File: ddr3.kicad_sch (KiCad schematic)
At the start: 26 parts, among them U11 LIFCL-40-9BG256C, U12 MT41K128M16JT-125_K

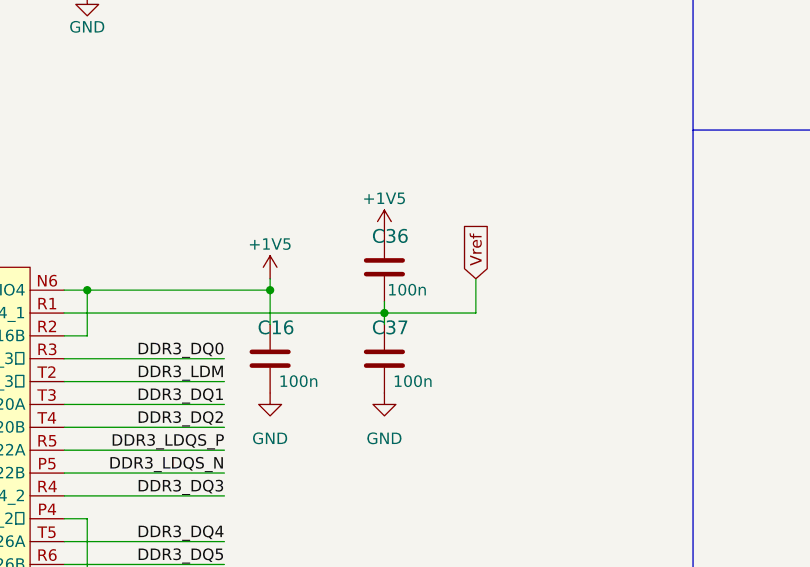
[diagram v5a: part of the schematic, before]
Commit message: Finished component placement
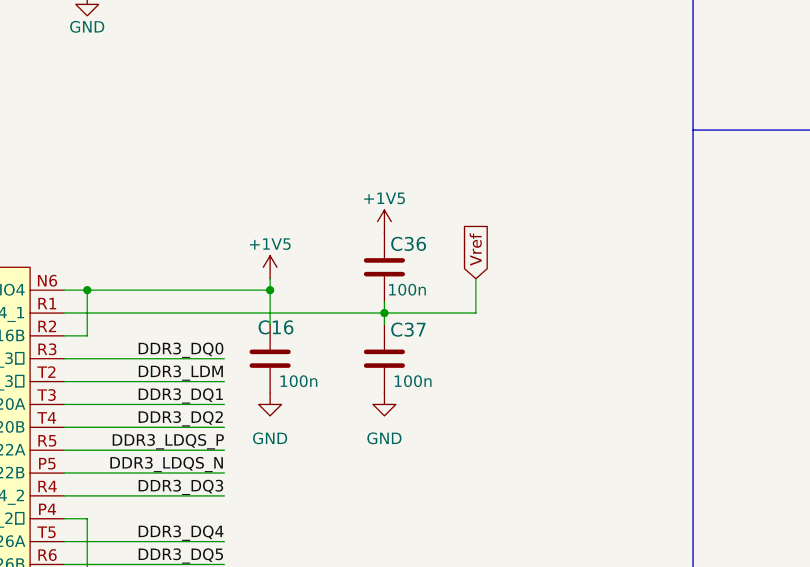
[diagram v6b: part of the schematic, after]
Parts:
- removed R43: R_100R_0402, crosslink-nx-video-converter-footprints:0402-res, symbol crosslink-nx-video-converter:R_100R_0402
- added R43: R_100R_0201, antmicro-footprints:0201-res, symbol antmicroResistorsmisc:R_100R_0201
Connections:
- net DDR3_CK_N: now also R43.1
- net DDR3_CK_P: now also R43.2
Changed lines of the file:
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@@
     (pin "8")
-  )
-  (symbol (lib_id "crosslink-nx-video-converter:R_100R_0402") (at 190.5 83.82 90) (unit 1)
-    (in_bom yes) (on_board yes) (fields_autoplaced)
-    (property "Reference" "R43" (id 0) (at 193.04 82.55 90)
-      (effects (font (size 1.524 1.524)) (justify right))
-    )
-    (property "Value" "R_100R_0402" (id 1) (at 194.31 83.82 0)
-      (effects (font (size 1.524 1.524)) hide)
-    )
-    (property "Footprint" "crosslink-nx-video-converter-footprints:0402-res" (id 2) (at 185.42 78.74 0)
-      (effects (font (size 1.524 1.524)) (justify left) hide)
-    )
-    (property "Datasheet" "" (id 3) (at 190.5 83.82 0)
-      (effects (font (size 1.27 1.27)) hide)
-    )
-    (property "Manufacturer" "BOURNS" (id 4) (at 180.34 78.74 0)
-      (effects (font (size 1.524 1.524)) (justify left) hide)
-    )
-    (property "MPN" "CR0402-FX-1000GLF" (id 5) (at 182.88 78.74 0)
-      (effects (font (size 1.524 1.524)) (justify left) hide)
-    )
-    (property "Val" "100R" (id 6) (at 193.04 85.7249 90)
-      (effects (font (size 1.27 1.27)) (justify right))
-    )
-    (pin "1")
-    (pin "2")
   )
   (symbol (lib_id "antmicroCapacitors0402:C_100n_0402") (at 130.81 181.61 0) (unit 1)
     (in_bom yes) (on_board yes)
-    (property "Reference" "C37" (id 0) (at 129.413 178.181 0)
+    (property "Reference" "C37" (id 0) (at 131.445 178.435 0)
       (effects (font (size 1.524 1.524)) (justify left))
     )
@@
     (pin "8")
   )
+  (symbol (lib_id "antmicroResistorsmisc:R_100R_0201") (at 190.5 83.82 90) (unit 1)
+    (in_bom yes) (on_board yes) (fields_autoplaced)
+    (property "Reference" "R43" (id 0) (at 193.04 82.55 90)
+      (effects (font (size 1.524 1.524)) (justify right))
+    )
+    (property "Value" "R_100R_0201" (id 1) (at 198.12 83.82 0)
+      (effects (font (size 1.524 1.524)) hide)
+    )
+    (property "Footprint" "antmicro-footprints:0201-res" (id 2) (at 205.74 95.25 0)
+      (effects (font (size 1.524 1.524)) (justify left) hide)
+    )
+    (property "Datasheet" "https://www.mouser.pl/datasheet/2/54/cr_a_as-1858644.pdf" (id 3) (at 195.58 83.82 0)
+      (effects (font (size 1.27 1.27)) hide)
+    )
+    (property "Manufacturer" "Bourns" (id 4) (at 200.66 95.25 0)
+      (effects (font (size 1.524 1.524)) (justify left) hide)
+    )
+    (property "MPN" "CR0201AFW-1000GAS " (id 5) (at 203.2 95.25 0)
+      (effects (font (size 1.524 1.524)) (justify left) hide)
+    )
+    (property "Val" "100R" (id 6) (at 193.04 85.7249 90)
+      (effects (font (size 1.27 1.27)) (justify right))
+    )
+    (pin "1")
+    (pin "2")
+  )
   (symbol (lib_id "power:GND") (at 295.91 87.63 0) (unit 1)
     (in_bom yes) (on_board yes) (fields_autoplaced)
@@
   (symbol (lib_id "antmicroCapacitors0402:C_100n_0402") (at 130.81 171.45 0) (unit 1)
     (in_bom yes) (on_board yes)
-    (property "Reference" "C36" (id 0) (at 129.413 168.021 0)
+    (property "Reference" "C36" (id 0) (at 131.445 168.91 0)
       (effects (font (size 1.524 1.524)) (justify left))
     )

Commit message: Loclib
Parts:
- C16, C35, C36, C37, C38, C39: footprint antmicro-footprints:0402-cap -> crosslink-nx-video-converter-footprints:0402-cap; symbol antmicroCapacitors0402:C_100n_0402 -> crosslink-nx-video-converter:C_100n_0402
- R43: footprint antmicro-footprints:0201-res -> crosslink-nx-video-converter-footprints:0201-res; symbol antmicroResistorsmisc:R_100R_0201 -> crosslink-nx-video-converter:R_100R_0201
- U11: footprint antmicro-footprints:BGA-256_16x16_14.0x14.0mm -> crosslink-nx-video-converter-footprints:BGA-256_16x16_14.0x14.0mm; symbol antmicroBGAchips:LIFCL-40-9BG256C -> crosslink-nx-video-converter:LIFCL-40-9BG256C
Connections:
- net +1V5: no longer U11.P11 (PB54B/PCLKC3_0/ADC_CN5 ), U11.P12 (VCCIO3)
- net DDR3_A0: no longer U11.N13 (PB70B/COMP2IN )
- net DDR3_A1: no longer U11.P15 (PB72A/PCLKT3_2/ADC_CP13)
- net DDR3_A10: no longer U11.L12 (PB82B/ADC_CN15)
- net DDR3_A11: no longer U11.M16 (PB84A/LRC_GPLL0T_IN)
- net DDR3_A2: no longer U11.P16 (PB72B/PCLKC3_2/ADC_CN13)
- net DDR3_A3: no longer U11.M14 (PB74A/PCLKT3_3/ADC_CP14)
- net DDR3_A4: no longer U11.N16 (PB76A/COMP3IP)
- net DDR3_A5: no longer U11.N15 (PB76B/COMP3IN)
- net DDR3_A6: no longer U11.M12 (PB78A/ADC_CP11)
- net DDR3_A7: no longer U11.L11 (PB80A/ADC_CP12)
- net DDR3_A8: no longer U11.L10 (PB80B/ADC_CN12)
- net DDR3_A9: no longer U11.M13 (PB82A/ADC_CP15)
- net DDR3_DQ10: no longer U11.T11 (PB58B/PCLKC3_1/ADC_CN6 )
- net DDR3_DQ11: no longer U11.R13 (PB62A/ADC_CP10)
- net DDR3_DQ12: no longer U11.R14 (PB62B/ADC_CN10)
- net DDR3_DQ13: no longer U11.T14 (PB66A/COMP1IP)
- net DDR3_DQ14: no longer U11.T15 (PB66B/COMP1IN)
- net DDR3_DQ15: no longer U11.R16 (PB68A/ADC_CP8)
- net DDR3_DQ8: no longer U11.R10 (PB56B/ADC_CN7 )
- net DDR3_DQ9: no longer U11.T12 (PB58A/PCLKT3_1/ADC_CP6 )
- net DDR3_UDM: no longer U11.R15 (PB68B/ADC_CN8)
- net DDR3_UDQS_N: no longer U11.T13 (PB60B/ADC_CN9)
- net DDR3_UDQS_P: no longer U11.R12 (PB60A/ADC_CP9)
- net GND: no longer U11.M11 (PB78B/ADC_CN11), U11.M15 (PB84B/LRC_GPLL0C_IN/VREF3_2), U11.N11 (PB64B/ADC_CN4), U11.N12 (PB64A/ADC_CP4), U11.N14 (PB74B/PCLKC3_3/ADC_CN14), U11.P10 (PB56A/ADC_CP7 ), U11.P14 (PB70A/COMP2IP)
- net Vref: no longer U11.R11 (PB54A/PCLKT3_0/VREF3_1/ADC_CP5)

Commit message: Routed DDR3 C&A
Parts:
- removed unit 4 of U11
- added unit 4 of U11
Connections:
- net +1V5: now also U11.P11 (PB54B/PCLKC3_0/ADC_CN5 ), U11.P12 (VCCIO3)
- net DDR3_A0: now also R49.4, U11.P8 (PB42B); no longer R44.1
- net DDR3_A1: now also R46.4, U11.N16 (PB76A/COMP3IP); no longer R44.2
- net DDR3_A10: now also R46.1, U11.P15 (PB72A/PCLKT3_2/ADC_CP13); no longer R46.3
- net DDR3_A11: now also R48.2, U11.M14 (PB74A/PCLKT3_3/ADC_CP14); no longer R46.4
- net DDR3_A12: now also R46.2, U11.N15 (PB76B/COMP3IN); no longer R48.1, U11.T7 (PB30A)
- net DDR3_A13: now also R49.1, U11.L11 (PB80A/ADC_CP12); no longer R48.2, U11.T8 (PB30B)
- net DDR3_A2: now also R49.2, U11.N8 (PB36A); no longer R44.3
- net DDR3_A3: now also R49.3, U11.P7 (PB32B); no longer R44.4
- net DDR3_A4: now also R48.1, U11.M16 (PB84A/LRC_GPLL0T_IN); no longer R45.1
- net DDR3_A5: now also R45.1, U11.N9 (PB36B); no longer R45.2
- net DDR3_A6: now also R48.3, U11.M13 (PB82A/ADC_CP15); no longer R45.3
- net DDR3_A7: now also R45.2, U11.L10 (PB80B/ADC_CN12); no longer R45.4
- net DDR3_A8: now also R48.4, U11.L12 (PB82B/ADC_CN15); no longer R46.1
- net DDR3_A9: now also R45.4, U11.L8 (PB34A); no longer R46.2
- net DDR3_BA0: now also R44.1, U11.P9 (PB44B/PCLKC4_0); no longer R48.3, U11.P6 (PB32A)
- net DDR3_BA1: now also R46.3, U11.P16 (PB72B/PCLKC3_2/ADC_CN13); no longer R48.4, U11.P7 (PB32B)
- net DDR3_BA2: now also R44.2, U11.M10 (PB46A); no longer R50.4, U11.L8 (PB34A)
- net DDR3_CKE: now also R50.4, U11.N13 (PB70B/COMP2IN ); no longer R50.3, U11.P9 (PB44B/PCLKC4_0)
- net DDR3_DQ0: now also U11.T4 (PB20B); no longer U11.R3 (PB18A/PCLKT4_3 )
- net DDR3_DQ1: now also U11.T6 (PB28A); no longer U11.T3 (PB20A)
- net DDR3_DQ10: now also U11.T15 (PB66B/COMP1IN)
- net DDR3_DQ11: now also U11.R13 (PB62A/ADC_CP10)
- net DDR3_DQ12: now also U11.R14 (PB62B/ADC_CN10)
- net DDR3_DQ13: now also U11.R10 (PB56B/ADC_CN7 )
- net DDR3_DQ14: now also U11.R15 (PB68B/ADC_CN8)
- net DDR3_DQ15: now also U11.T11 (PB58B/PCLKC3_1/ADC_CN6 )
- net DDR3_DQ2: now also U11.R3 (PB18A/PCLKT4_3 ); no longer U11.T4 (PB20B)
- net DDR3_DQ3: now also U11.R6 (PB26B); no longer U11.R4 (PB24A/PCLKT4_2)
- net DDR3_DQ4: now also U11.T2 (PB18B/PCLKC4_3 ); no longer U11.T5 (PB26A)
- net DDR3_DQ5: now also U11.R4 (PB24A/PCLKT4_2); no longer U11.R6 (PB26B)
- net DDR3_DQ6: now also U11.T3 (PB20A); no longer U11.T6 (PB28A)
- net DDR3_DQ7: now also U11.T5 (PB26A); no longer U11.R7 (PB28B)
- net DDR3_DQ8: now also U11.R16 (PB68A/ADC_CP8)
- net DDR3_DQ9: now also U11.T12 (PB58A/PCLKT3_1/ADC_CP6 )
- net DDR3_LDM: now also U11.R7 (PB28B); no longer U11.T2 (PB18B/PCLKC4_3 )
- net DDR3_ODT: now also R50.1, U11.T7 (PB30A); no longer R50.2, U11.M10 (PB46A)
- net DDR3_UDM: now also U11.T14 (PB66A/COMP1IP)
- net DDR3_UDQS_N: now also U11.T13 (PB60B/ADC_CN9)
- net DDR3_UDQS_P: now also U11.R12 (PB60A/ADC_CP9)
- net GND: now also U11.M11 (PB78B/ADC_CN11), U11.M15 (PB84B/LRC_GPLL0C_IN/VREF3_2), U11.N11 (PB64B/ADC_CN4), U11.N12 (PB64A/ADC_CP4), U11.N14 (PB74B/PCLKC3_3/ADC_CN14), U11.P10 (PB56A/ADC_CP7 ), U11.P14 (PB70A/COMP2IP)
- net Vref: now also U11.R11 (PB54A/PCLKT3_0/VREF3_1/ADC_CP5)
- net ~{DDR3_CAS}: now also R50.2, U11.T8 (PB30B); no longer R49.3, U11.N8 (PB36A)
- net ~{DDR3_CS}: now also R44.3, U11.N10 (PB46B/VREF4_2); no longer R50.1, U11.P8 (PB42B)
- net ~{DDR3_RAS}: now also R50.3, U11.M12 (PB78A/ADC_CP11); no longer R49.2, U11.L9 (PB34B)
- net ~{DDR3_RESET}: now also R45.3, U11.L9 (PB34B); no longer R49.1, U11.N10 (PB46B/VREF4_2)
- net ~{DDR3_WE}: now also R44.4, U11.P6 (PB32A); no longer R49.4, U11.N9 (PB36B)
